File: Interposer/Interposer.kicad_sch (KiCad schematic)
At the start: 9 parts, among them J1 Cis_Electrode_In, J10 Trans_Electrode_Out, J11 Trans_Electrode_In, J2 Cis_Electrode_Out

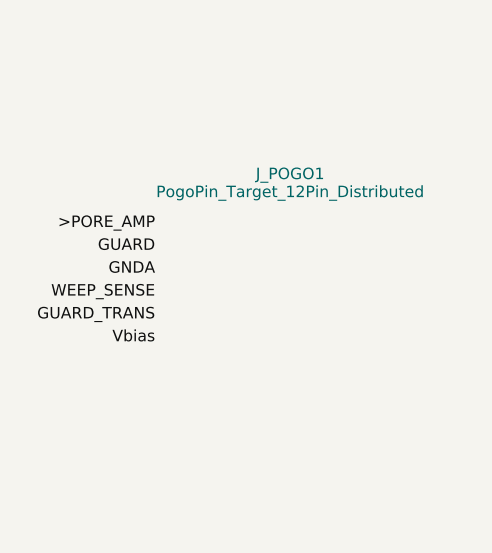
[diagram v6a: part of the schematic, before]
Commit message: feat: Add Path 2 wideband TIA channel for 200nm pores
Co-authored-by: google-labs-jules[bot] <161369871+google-labs-jules[bot]@users.noreply.github.com>
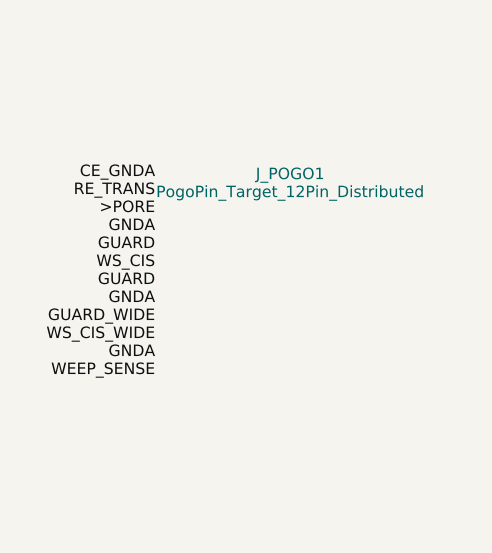
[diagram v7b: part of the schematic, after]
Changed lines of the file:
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@@
 		(pin "2")
 	)
-	(label ">PORE_AMP" (at 55.0 73.66 180) (effects (font (size 1.27 1.27))))
-	(label "GUARD" (at 55.0 76.2 180) (effects (font (size 1.27 1.27))))
-	(label "GNDA" (at 55.0 78.74 180) (effects (font (size 1.27 1.27))))
-	(label "WEEP_SENSE" (at 55.0 81.28 180) (effects (font (size 1.27 1.27))))
-	(label "GUARD_TRANS" (at 55.0 83.82 180) (effects (font (size 1.27 1.27))))
-	(label "Vbias" (at 55.0 86.36 180) (effects (font (size 1.27 1.27))))
+	(label "CE_GNDA" (at 55.0 68.0 180) (effects (font (size 1.27 1.27))))
+	(label "RE_TRANS" (at 55.0 70.0 180) (effects (font (size 1.27 1.27))))
+	(label ">PORE" (at 55.0 72.0 180) (effects (font (size 1.27 1.27))))
+	(label "GNDA" (at 55.0 74.0 180) (effects (font (size 1.27 1.27))))
+	(label "GUARD" (at 55.0 76.0 180) (effects (font (size 1.27 1.27))))
+	(label "WS_CIS" (at 55.0 78.0 180) (effects (font (size 1.27 1.27))))
+	(label "GUARD" (at 55.0 80.0 180) (effects (font (size 1.27 1.27))))
+	(label "GNDA" (at 55.0 82.0 180) (effects (font (size 1.27 1.27))))
+	(label "GUARD_WIDE" (at 55.0 84.0 180) (effects (font (size 1.27 1.27))))
+	(label "WS_CIS_WIDE" (at 55.0 86.0 180) (effects (font (size 1.27 1.27))))
+	(label "GNDA" (at 55.0 88.0 180) (effects (font (size 1.27 1.27))))
+	(label "WEEP_SENSE" (at 55.0 90.0 180) (effects (font (size 1.27 1.27))))
 	(label ">PORE_AMP" (at 210.0 57.46 0) (effects (font (size 1.27 1.27))))
 	(label "GUARD" (at 210.0 60.0 0) (effects (font (size 1.27 1.27))))

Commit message: adding new symbols
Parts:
- removed J_POGO1: PogoPin_Target_12Pin_Distributed, footprints:PogoPin_Target_12Pin_Distributed, symbol Connector_Generic:Conn_01x12
- added J_POGO1: PogoPin_Target_6Pin_Cis, footprints:PogoPin_Target_6Pin_Cis, symbol Connector_Generic:Conn_01x06
- added J_POGO2: PogoPin_Target_6Pin_Trans, footprints:PogoPin_Target_6Pin_Trans, symbol Connector_Generic:Conn_01x06
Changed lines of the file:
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@@
 		(comment 4 "Dual-Sided Ag/AgCl Ribbon Electrode Contacts with Weep Moat Leak Detection")
 	)
-	(symbol (lib_id "Connector_Generic:Conn_01x12") (at 70.0 80.0 0) (unit 1)
-		(property "Reference" "J_POGO1" (at 70.0 68.0 0) (effects (font (size 1.27 1.27))))
-		(property "Value" "PogoPin_Target_12Pin_Distributed" (at 70.0 70.0 0) (effects (font (size 1.27 1.27))))
-		(property "Footprint" "footprints:PogoPin_Target_12Pin_Distributed" (at 70.0 80.0 0) (hide yes) (effects (font (size 1.27 1.27))))
+	(symbol (lib_id "Connector_Generic:Conn_01x06") (at 70.0 70 0) (unit 1)
+		(property "Reference" "J_POGO1" (at 70.0 58 0) (effects (font (size 1.27 1.27))))
+		(property "Value" "PogoPin_Target_6Pin_Cis" (at 70.0 60 0) (effects (font (size 1.27 1.27))))
+		(property "Footprint" "footprints:PogoPin_Target_6Pin_Cis" (at 70.0 70 0) (hide yes) (effects (font (size 1.27 1.27))))
 		(pin "1")
 		(pin "2")
@@
 		(pin "5")
 		(pin "6")
-		(pin "7")
-		(pin "8")
-		(pin "9")
-		(pin "10")
-		(pin "11")
-		(pin "12")
+	)
+	(symbol (lib_id "Connector_Generic:Conn_01x06") (at 70.0 100 0) (unit 1)
+		(property "Reference" "J_POGO2" (at 70.0 88 0) (effects (font (size 1.27 1.27))))
+		(property "Value" "PogoPin_Target_6Pin_Trans" (at 70.0 90 0) (effects (font (size 1.27 1.27))))
+		(property "Footprint" "footprints:PogoPin_Target_6Pin_Trans" (at 70.0 100 0) (hide yes) (effects (font (size 1.27 1.27))))
+		(pin "1")
+		(pin "2")
+		(pin "3")
+		(pin "4")
+		(pin "5")
+		(pin "6")
 	)
 	(symbol (lib_id "Mechanical:MountingHole") (at 140.0 80.0 0) (unit 1)
@@
 		(pin "2")
 	)
-	(label "CE_GNDA" (at 55.0 68.0 180) (effects (font (size 1.27 1.27))))
-	(label "RE_TRANS" (at 55.0 70.0 180) (effects (font (size 1.27 1.27))))
-	(label ">PORE" (at 55.0 72.0 180) (effects (font (size 1.27 1.27))))
-	(label "GNDA" (at 55.0 74.0 180) (effects (font (size 1.27 1.27))))
-	(label "GUARD" (at 55.0 76.0 180) (effects (font (size 1.27 1.27))))
-	(label "WS_CIS" (at 55.0 78.0 180) (effects (font (size 1.27 1.27))))
-	(label "GUARD" (at 55.0 80.0 180) (effects (font (size 1.27 1.27))))
-	(label "GNDA" (at 55.0 82.0 180) (effects (font (size 1.27 1.27))))
-	(label "GUARD_WIDE" (at 55.0 84.0 180) (effects (font (size 1.27 1.27))))
-	(label "WS_CIS_WIDE" (at 55.0 86.0 180) (effects (font (size 1.27 1.27))))
-	(label "GNDA" (at 55.0 88.0 180) (effects (font (size 1.27 1.27))))
-	(label "WEEP_SENSE" (at 55.0 90.0 180) (effects (font (size 1.27 1.27))))
+	(label "GNDA" (at 55.0 65 180) (effects (font (size 1.27 1.27))))
+	(label ">PORE_AMP" (at 55.0 67 180) (effects (font (size 1.27 1.27))))
+	(label "GNDA" (at 55.0 69 180) (effects (font (size 1.27 1.27))))
+	(label "GUARD" (at 55.0 71 180) (effects (font (size 1.27 1.27))))
+	(label "GNDA" (at 55.0 73 180) (effects (font (size 1.27 1.27))))
+	(label "WEEP_SENSE" (at 55.0 75 180) (effects (font (size 1.27 1.27))))
+	(label "CE_GNDA" (at 55.0 95 180) (effects (font (size 1.27 1.27))))
+	(label "RE_TRANS" (at 55.0 97 180) (effects (font (size 1.27 1.27))))
+	(label "GUARD_WIDE" (at 55.0 99 180) (effects (font (size 1.27 1.27))))
+	(label "WS_CIS_WIDE" (at 55.0 101 180) (effects (font (size 1.27 1.27))))
+	(label "GUARD" (at 55.0 103 180) (effects (font (size 1.27 1.27))))
+	(label "WS_CIS" (at 55.0 105 180) (effects (font (size 1.27 1.27))))
 	(label ">PORE_AMP" (at 210.0 57.46 0) (effects (font (size 1.27 1.27))))
 	(label "GUARD" (at 210.0 60.0 0) (effects (font (size 1.27 1.27))))
